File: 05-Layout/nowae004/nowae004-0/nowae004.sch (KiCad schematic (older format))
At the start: 30 parts

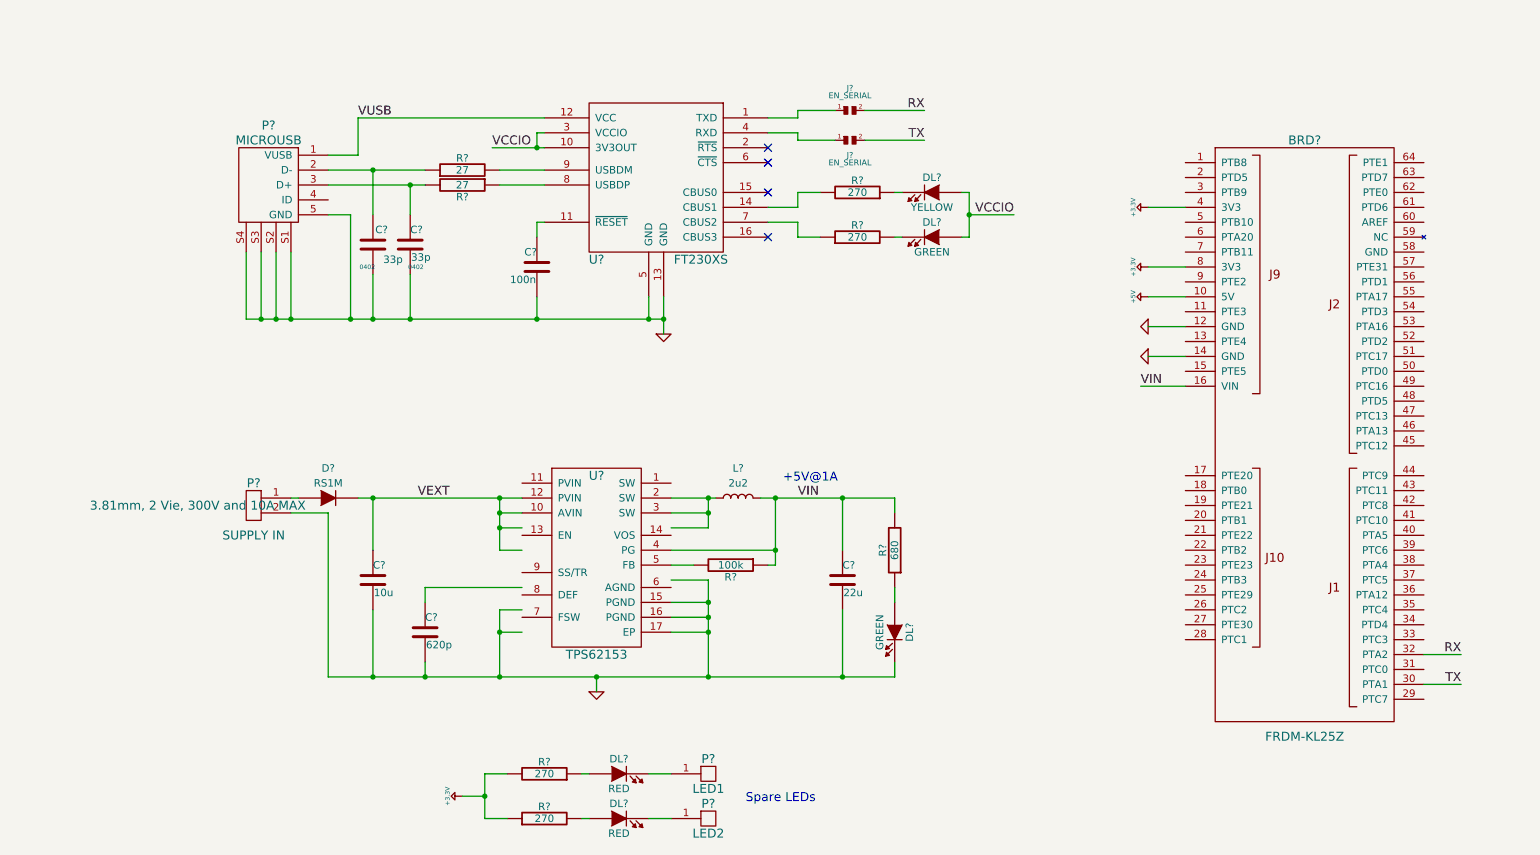
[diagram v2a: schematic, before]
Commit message: Added enumeration into schematich
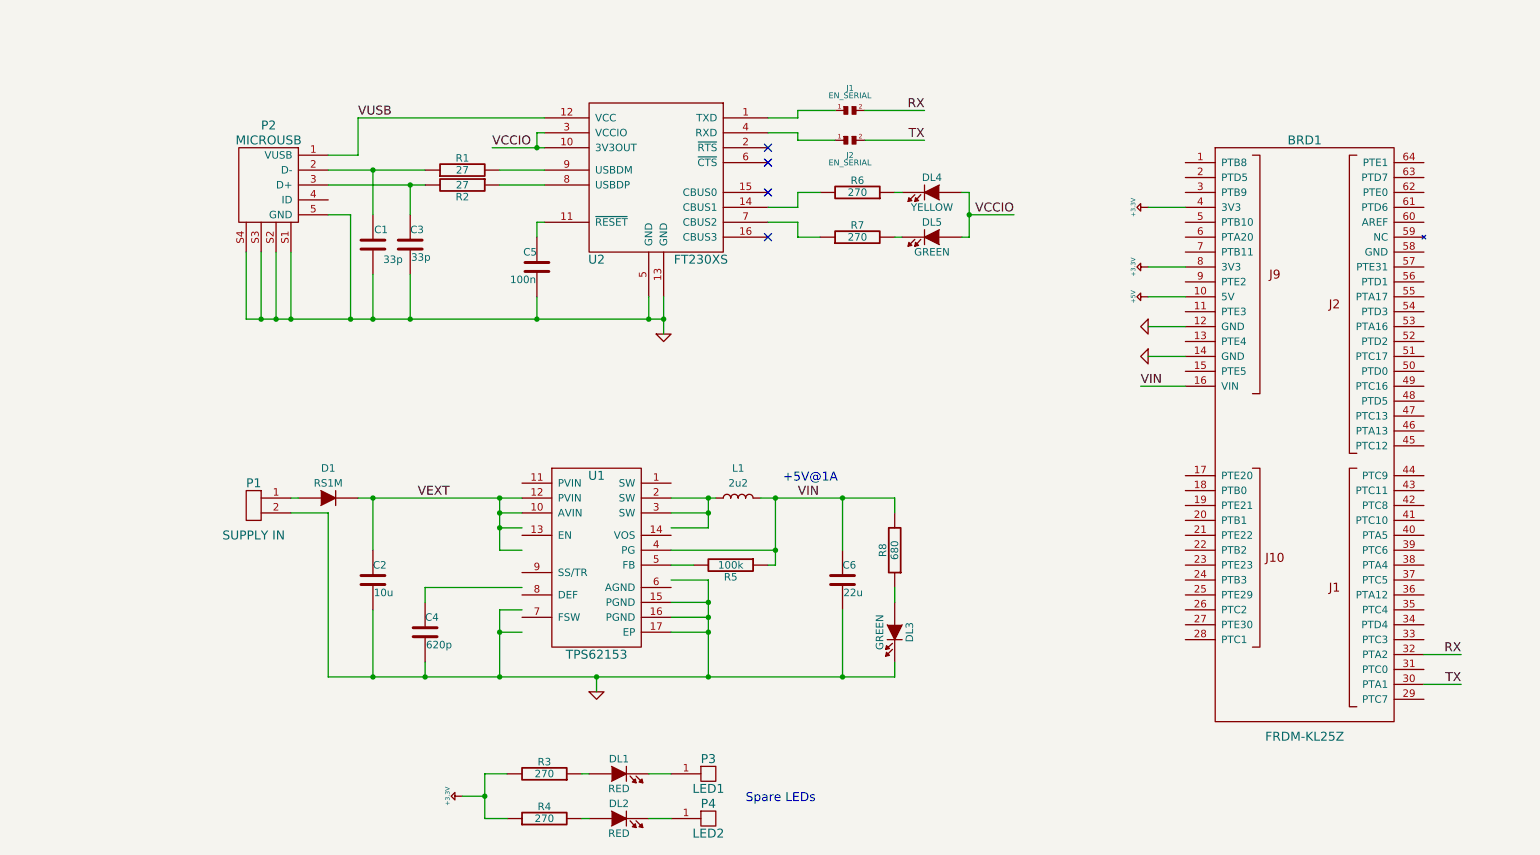
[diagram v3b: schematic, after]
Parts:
- gave numbers to parts that had none: 30
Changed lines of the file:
@@
 Comment2 "Nicola Orlandini"
 Comment3 "Nicola Orlandini"
-Comment4 "2017-02-24"
+Comment4 "2017-02-28"
 $EndDescr
 $Comp
-L GREEN DL?
+L GREEN DL5
 U 1 1 589DB2EE
 P 8500 4000
-F 0 "DL?" H 8500 4100 50  0000 C CNN
+F 0 "DL5" H 8500 4100 50  0000 C CNN
 F 1 "GREEN" H 8500 3900 50  0000 C CNN
 F 2 "0603" H 8500 4000 60  0001 C CNN
@@
 $EndComp
 $Comp
-L YELLOW DL?
+L YELLOW DL4
 U 1 1 589DB33F
 P 8500 3700
-F 0 "DL?" H 8500 3800 50  0000 C CNN
+F 0 "DL4" H 8500 3800 50  0000 C CNN
 F 1 "YELLOW" H 8500 3600 50  0000 C CNN
 F 2 "" H 8500 3700 60  0001 C CNN
@@
 $EndComp
 $Comp
-L RESISTOR R?
+L RESISTOR R7
 U 1 1 589DBA27
 P 8000 4000
-F 0 "R?" V 8080 4000 50  0000 C CNN
+F 0 "R7" V 8080 4000 50  0000 C CNN
 F 1 "270" V 8000 4000 50  0000 C CNN
 F 2 "0402" V 7930 4000 30  0001 C CNN
@@
 VCCIO
 $Comp
-L CAPACITOR C?
+L CAPACITOR C5
 U 1 1 589DBD48
 P 5850 4200
-F 0 "C?" H 5850 4300 50  0000 L CNN
+F 0 "C5" H 5850 4300 50  0000 L CNN
 F 1 "100n" H 5856 4115 50  0000 L CNN
 F 2 "0402" H 5888 4050 30  0001 C CNN
@@
 	6600 4550 6700 4550
 $Comp
-L RESISTOR R?
+L RESISTOR R2
 U 1 1 589DC009
 P 5350 3650
-F 0 "R?" V 5430 3650 50  0000 C CNN
+F 0 "R2" V 5430 3650 50  0000 C CNN
 F 1 "27" V 5350 3650 50  0000 C CNN
 F 2 "0402" V 5280 3650 30  0001 C CNN
@@
 $EndComp
 $Comp
-L RESISTOR R?
+L RESISTOR R1
 U 1 1 589DC06A
 P 5350 3550
-F 0 "R?" V 5430 3550 50  0000 C CNN
+F 0 "R1" V 5430 3550 50  0000 C CNN
 F 1 "27" V 5350 3550 50  0000 C CNN
 F 2 "0402" V 5280 3550 30  0001 C CNN
@@
 $EndComp
 $Comp
-L CAPACITOR C?
+L CAPACITOR C3
 U 1 1 589DC137
 P 5000 4050
-F 0 "C?" H 5000 4150 50  0000 L CNN
+F 0 "C3" H 5000 4150 50  0000 L CNN
 F 1 "33p" H 5006 3965 50  0000 L CNN
-F 2 "0402" H 5038 3900 30  0000 C CNN
+F 2 "0402" H 5038 3900 30  0001 C CNN
 F 3 "" H 5000 4050 60  0000 C CNN
 F 4 "Multicomp" H 4550 5950 60  0001 C CNN "Manufacturer"
@@
 $EndComp
 $Comp
-L CAPACITOR C?
+L CAPACITOR C1
 U 1 1 589DC176
 P 4750 4050
-F 0 "C?" H 4650 4150 50  0000 L CNN
+F 0 "C1" H 4650 4150 50  0000 L CNN
 F 1 "33p" H 4550 3950 50  0000 L CNN
-F 2 "0402" H 4788 3900 30  0000 C CNN
+F 2 "0402" H 4788 3900 30  0001 C CNN
 F 3 "" H 4750 4050 60  0000 C CNN
 F 4 "Multicomp" H 4550 5950 60  0001 C CNN "Manufacturer"
@@
 Connection ~ 5000 4550
 $Comp
-L RESISTOR R?
+L RESISTOR R6
 U 1 1 589DB816
 P 8000 3700
-F 0 "R?" V 8080 3700 50  0000 C CNN
+F 0 "R6" V 8080 3700 50  0000 C CNN
 F 1 "270" V 8000 3700 50  0000 C CNN
 F 2 "0402" V 7930 3700 30  0001 C CNN
@@
 	7600 3350 7850 3350
 $Comp
-L SMALL_JUMPER J?
+L SMALL_JUMPER J2
 U 1 1 58ACFDE1
 P 7950 3350
-F 0 "J?" H 7950 3250 39  0000 C CNN
+F 0 "J2" H 7950 3250 39  0000 C CNN
 F 1 "EN_SERIAL" H 7950 3200 39  0000 C CNN
 F 2 "" H 7950 3350 60  0000 C CNN
@@
 $EndComp
 $Comp
-L SMALL_JUMPER J?
+L SMALL_JUMPER J1
 U 1 1 58AD00EA
 P 7950 3150
-F 0 "J?" H 7950 3300 39  0000 C CNN
+F 0 "J1" H 7950 3300 39  0000 C CNN
 F 1 "EN_SERIAL" H 7950 3250 39  0000 C CNN
 F 2 "" H 7950 3150 60  0000 C CNN
@@
 Connection ~ 6700 4550
 $Comp
-L GND #PWR?
+L GND #PWR3
 U 1 1 58AD26EE
 P 6700 4650
-F 0 "#PWR?" H 6700 4650 30  0001 C CNN
+F 0 "#PWR3" H 6700 4650 30  0001 C CNN
 F 1 "GND" H 6700 4650 30  0001 C CNN
 F 2 "" H 6700 4650 60  0000 C CNN
@@
 	4600 3850 4600 4550
 $Comp
-L FRDM-KL25Z BRD?
+L FRDM-KL25Z BRD1
 U 1 1 58AD8FDC
 P 11000 5500
-F 0 "BRD?" H 11000 7650 60  0000 C CNN
+F 0 "BRD1" H 11000 7650 60  0000 C CNN
 F 1 "FRDM-KL25Z" H 11000 3650 60  0000 C CNN
 F 2 "" H 10700 5900 60  0000 C CNN
@@
 	10200 4800 9950 4800
 $Comp
-L GND #PWR?
+L GND #PWR7
 U 1 1 58AD94F9
 P 9950 4600
-F 0 "#PWR?" H 9950 4600 30  0001 C CNN
+F 0 "#PWR7" H 9950 4600 30  0001 C CNN
 F 1 "GND" H 9950 4600 30  0001 C CNN
 F 2 "" H 9950 4600 60  0000 C CNN
@@
 $EndComp
 $Comp
-L GND #PWR?
+L GND #PWR8
 U 1 1 58AD9532
 P 9950 4800
-F 0 "#PWR?" H 9950 4800 30  0001 C CNN
+F 0 "#PWR8" H 9950 4800 30  0001 C CNN
 F 1 "GND" H 9950 4800 30  0001 C CNN
 F 2 "" H 9950 4800 60  0000 C CNN
@@
 	10200 3800 9950 3800
 $Comp
-L +3.3V #PWR?
+L +3.3V #PWR4
 U 1 1 58AD96A9
 P 9950 3800
-F 0 "#PWR?" H 9950 3725 30  0001 C CNN
+F 0 "#PWR4" H 9950 3725 30  0001 C CNN
 F 1 "+3.3V" H 9950 3900 30  0000 C CNN
 F 2 "" H 9950 3800 60  0000 C CNN
@@
 $EndComp
 $Comp
-L +3.3V #PWR?
+L +3.3V #PWR5
 U 1 1 58AD96E2
 P 9950 4200
-F 0 "#PWR?" H 9950 4125 30  0001 C CNN
+F 0 "#PWR5" H 9950 4125 30  0001 C CNN
 F 1 "+3.3V" H 9950 4300 30  0000 C CNN
 F 2 "" H 9950 4200 60  0000 C CNN
@@
 $EndComp
 $Comp
-L +5V #PWR?
+L +5V #PWR6
 U 1 1 58AD9709
 P 9950 4400
-F 0 "#PWR?" H 9950 4325 30  0001 C CNN
+F 0 "#PWR6" H 9950 4325 30  0001 C CNN
 F 1 "+5V" H 9950 4500 30  0000 C CNN
 F 2 "" H 9950 4400 60  0000 C CNN
@@
 $EndComp
 $Comp
-L MICROUSB-629105150521 P?
+L MICROUSB-629105150521 P2
 U 1 1 58AD9919
 P 4050 3650
-F 0 "P?" H 4050 4050 60  0000 C CNN
+F 0 "P2" H 4050 4050 60  0000 C CNN
 F 1 "MICROUSB" H 4050 3950 60  0000 C CNN
 F 2 "" H 4425 3650 60  0000 C CNN
@@
 Connection ~ 4200 4550
 $Comp
-L TPS62153 U?
+L TPS62153 U1
 U 1 1 58AED925
 P 6250 6200
-F 0 "U?" H 6250 6800 60  0000 C CNN
+F 0 "U1" H 6250 6800 60  0000 C CNN
 F 1 "TPS62153" H 6250 5600 60  0000 C CNN
 F 2 "VQFN16" H 6250 5100 60  0001 C CNN
@@
 $EndComp
 $Comp
-L CONN_2X1 P?
+L CONN_2X1 P1
 U 1 1 58AEDA14
 P 3950 5800
-F 0 "P?" H 3950 5950 60  0000 C CNN
+F 0 "P1" H 3950 5950 60  0000 C CNN
 F 1 "SUPPLY IN" H 3950 5600 60  0000 C CNN
 F 2 "" H 4325 5800 60  0000 C CNN
-F 3 "3.81mm, 2 Vie, 300V and 10A MAX " H 4325 5800 60  0000 C CNN
+F 3 "3.81mm, 2 Vie, 300V and 10A MAX " H 4325 5800 60  0001 C CNN
 F 4 "Multicomp" H 4550 5950 60  0001 C CNN "Manufacturer"
 F 5 "MC000018" H 4650 6050 60  0001 C CNN "Part Number"
@@
 Connection ~ 5600 6950
 $Comp
-L CAPACITOR C?
+L CAPACITOR C2
 U 1 1 58AEDD67
 P 4750 6300
-F 0 "C?" H 4750 6400 50  0000 L CNN
+F 0 "C2" H 4750 6400 50  0000 L CNN
 F 1 "10u" H 4756 6215 50  0000 L CNN
 F 2 "1206" H 4788 6150 30  0001 C CNN
@@
 Connection ~ 4750 6950
 $Comp
-L CAPACITOR C?
+L CAPACITOR C4
 U 1 1 58AEDFEA
 P 5100 6650
-F 0 "C?" H 5100 6750 50  0000 L CNN
+F 0 "C4" H 5100 6750 50  0000 L CNN
 F 1 "620p" H 5106 6565 50  0000 L CNN
 F 2 "0805" H 5138 6500 30  0001 C CNN
@@
 Connection ~ 7000 6450
 $Comp
-L CAPACITOR C?
+L CAPACITOR C6
 U 1 1 58AEE473
 P 7900 6300
-F 0 "C?" H 7900 6400 50  0000 L CNN
+F 0 "C6" H 7900 6400 50  0000 L CNN
 F 1 "22u" H 7906 6215 50  0000 L CNN
 F 2 "1206" H 7938 6150 30  0001 C CNN
@@
 Connection ~ 7000 6950
 $Comp
-L INDUCTOR L?
+L INDUCTOR L1
 U 1 1 58AEE57C
 P 7200 5750
-F 0 "L?" V 7400 5750 50  0000 C CNN
+F 0 "L1" V 7400 5750 50  0000 C CNN
 F 1 "2u2" V 7300 5750 50  0000 C CNN
 F 2 "" H 7200 5750 60  0000 C CNN
@@
 Connection ~ 7450 5750
 $Comp
-L RESISTOR R?
+L RESISTOR R5
 U 1 1 58AEE920
 P 7150 6200
-F 0 "R?" V 7230 6200 50  0000 C CNN
+F 0 "R5" V 7230 6200 50  0000 C CNN
 F 1 "100k" V 7150 6200 50  0000 C CNN
 F 2 "0402" V 7080 6200 30  0001 C CNN
@@
 Connection ~ 6250 6950
 $Comp
-L GND #PWR?
+L GND #PWR2
 U 1 1 58AEEF34
 P 6250 7050
-F 0 "#PWR?" H 6250 7050 30  0001 C CNN
+F 0 "#PWR2" H 6250 7050 30  0001 C CNN
 F 1 "GND" H 6250 7050 30  0001 C CNN
 F 2 "" H 6250 7050 60  0000 C CNN
@@
 Connection ~ 7900 5750
 $Comp
-L RESISTOR R?
+L RESISTOR R8
 U 1 1 58AEFD7A
 P 8250 6100
-F 0 "R?" V 8330 6100 50  0000 C CNN
+F 0 "R8" V 8330 6100 50  0000 C CNN
 F 1 "680" V 8250 6100 50  0000 C CNN
 F 2 "0402" V 8180 6100 30  0001 C CNN
@@
 	8250 5750 8250 5850
 $Comp
-L GREEN DL?
+L GREEN DL3
 U 1 1 58AEFE67
 P 8250 6650
-F 0 "DL?" H 8250 6750 50  0000 C CNN
+F 0 "DL3" H 8250 6750 50  0000 C CNN
 F 1 "GREEN" H 8250 6550 50  0000 C CNN
 F 2 "" H 8250 6650 60  0001 C CNN
@@
 	8250 6450 8250 6350
 $Comp
-L FT230XS U?
+L FT230XS U2
 U 1 1 58AF0874
 P 6650 3600
-F 0 "U?" H 6250 3050 60  0000 C CNN
+F 0 "U2" H 6250 3050 60  0000 C CNN
 F 1 "FT230XS" H 6950 3050 60  0000 C CNN
 F 2 "SSOP16" H 7000 4750 60  0001 C CNN
@@
 	4650 3200 5900 3200
 $Comp
-L RESISTOR R?
+L RESISTOR R4
 U 1 1 58B03137
 P 5900 7900
-F 0 "R?" V 5980 7900 50  0000 C CNN
+F 0 "R4" V 5980 7900 50  0000 C CNN
 F 1 "270" V 5900 7900 50  0000 C CNN
 F 2 "0402" V 5830 7900 30  0001 C CNN
@@
 	6150 7900 6200 7900
 $Comp
-L RESISTOR R?
+L RESISTOR R3
 U 1 1 58B03144
 P 5900 7600
-F 0 "R?" V 5980 7600 50  0000 C CNN
+F 0 "R3" V 5980 7600 50  0000 C CNN
 F 1 "270" V 5900 7600 50  0000 C CNN
 F 2 "0402" V 5830 7600 30  0001 C CNN
@@
 	5500 7900 5650 7900
 $Comp
-L RED DL?
+L RED DL1
 U 1 1 58B03399
 P 6400 7600
-F 0 "DL?" H 6400 7700 50  0000 C CNN
+F 0 "DL1" H 6400 7700 50  0000 C CNN
 F 1 "RED" H 6400 7500 50  0000 C CNN
 F 2 "0603" H 6400 7600 60  0001 C CNN
@@
 $EndComp
 $Comp
-L RED DL?
+L RED DL2
 U 1 1 58B03403
 P 6400 7900
-F 0 "DL?" H 6400 8000 50  0000 C CNN
+F 0 "DL2" H 6400 8000 50  0000 C CNN
 F 1 "RED" H 6400 7800 50  0000 C CNN
 F 2 "0603" H 6400 7900 60  0001 C CNN
@@
 Connection ~ 5500 7750
 $Comp
-L +3.3V #PWR?
+L +3.3V #PWR1
 U 1 1 58B03696
 P 5350 7750
-F 0 "#PWR?" H 5350 7675 30  0001 C CNN
+F 0 "#PWR1" H 5350 7675 30  0001 C CNN
 F 1 "+3.3V" H 5350 7850 30  0000 C CNN
 F 2 "" H 5350 7750 60  0000 C CNN
@@
 Spare LEDs
 $Comp
-L CONN_1X1 P?
+L CONN_1X1 P3
 U 1 1 58B04044
 P 7000 7600
-F 0 "P?" H 7000 7700 60  0000 C CNN
+F 0 "P3" H 7000 7700 60  0000 C CNN
 F 1 "LED1" H 7000 7500 60  0000 C CNN
 F 2 "" H 7375 7600 60  0000 C CNN
@@
 $EndComp
 $Comp
-L CONN_1X1 P?
+L CONN_1X1 P4
 U 1 1 58B041D9
 P 7000 7900
-F 0 "P?" H 7000 8000 60  0000 C CNN
+F 0 "P4" H 7000 8000 60  0000 C CNN
 F 1 "LED2" H 7000 7800 60  0000 C CNN
 F 2 "" H 7000 7700 60  0001 C CNN
@@
 $EndComp
 $Comp
-L RS1M D?
+L RS1M D1
 U 1 1 58B0468B
 P 4450 5750
-F 0 "D?" H 4450 5950 50  0000 C CNN
+F 0 "D1" H 4450 5950 50  0000 C CNN
 F 1 "RS1M" H 4450 5850 50  0000 C CNN
 F 2 "" H 4450 5750 60  0001 C CNN

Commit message: NOWAE004: Changed symbol of switching component
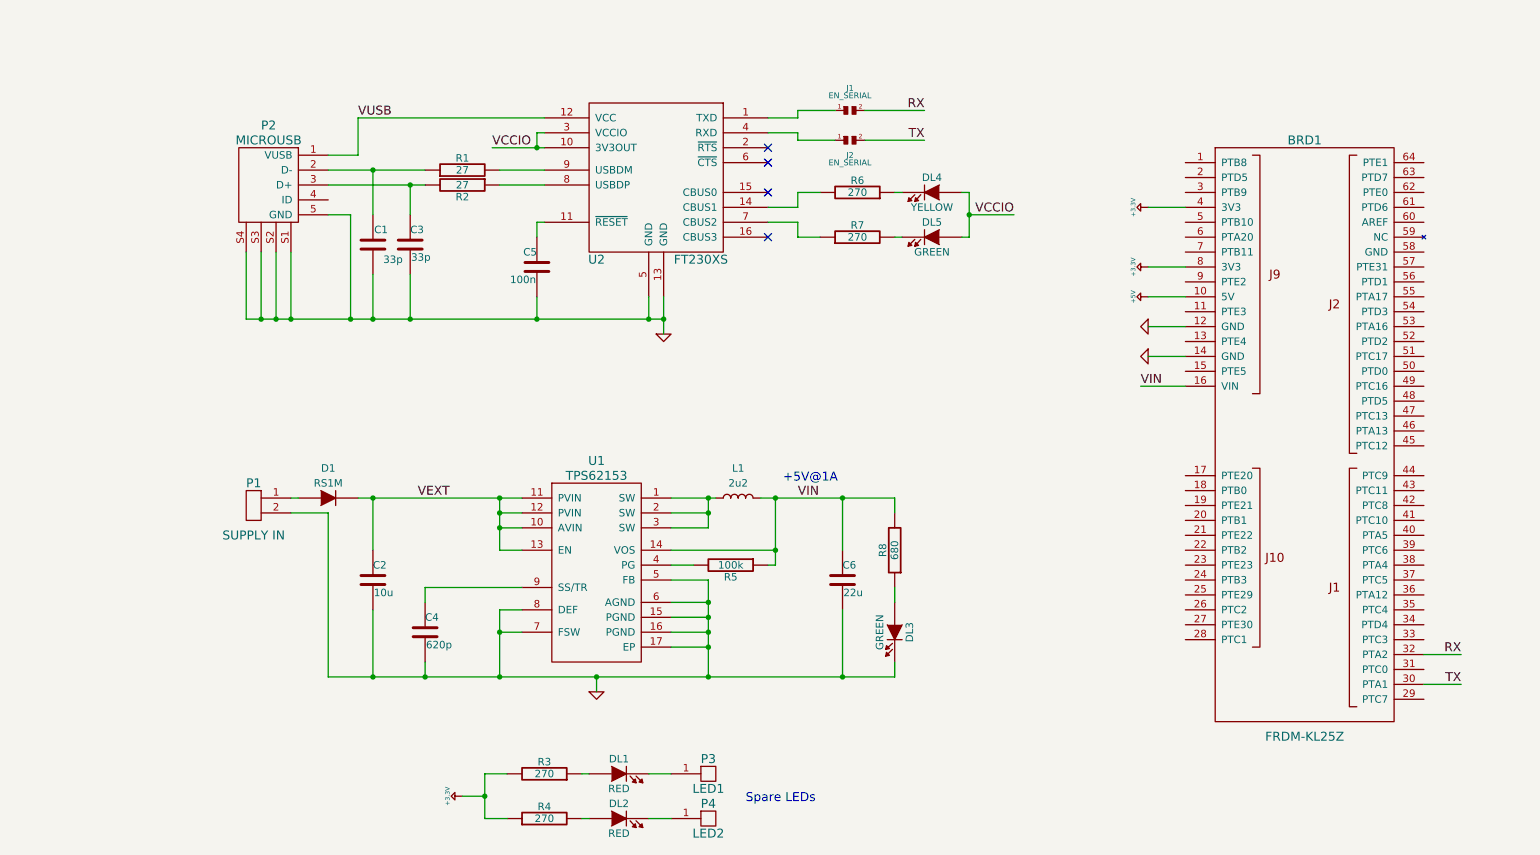
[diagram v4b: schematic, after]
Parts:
- BRD1: footprint (none) -> CONNECTOR:CONN-FRDM
- C1, C3, C5: footprint 0402 -> CAPACITOR:CAPACITOR-0402
- C2, C6: footprint 1206 -> CAPACITOR:CAPACITOR-1206
- C4: footprint 0805 -> CAPACITOR:CAPACITOR-0402
- D1: footprint (none) -> DIODE:DIODE-DO214AC-UNI
- DL1, DL2, DL5: footprint 0603 -> LEDs:LED-0603
- DL3, DL4: footprint (none) -> LEDs:LED-0603
- L1: footprint (none) -> INDUCTOR:INDUCTOR-TDK-SPM3012
- P1: footprint (none) -> CONNECTOR_MKDS:CONN-MKDS1_2-3.81
- P2: footprint (none) -> CONNECTOR:MICROUSB-WURTH-WRCOM
- R1, R2, R3, R4, R5, R6, R7, R8: footprint 0402 -> RESISTOR:RESISTOR-0402
- U1: footprint VQFN16 -> QFN:QFN16_3x3_0.5_16+1
- U2: footprint SSOP16 -> SSOP:SSOP16_3.9x4.9_0.635
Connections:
- wire segments 132 -> 100

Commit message: NOWAE004: Added last footprint and updated netlist
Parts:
- J1, J2: footprint (none) -> MISC:JUMPERSMD-2
- P3, P4: footprint (none) -> CONNECTOR:CONN-HOLE-1.2
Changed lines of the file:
@@
 F 0 "J2" H 7950 3250 39  0000 C CNN
 F 1 "EN_SERIAL" H 7950 3200 39  0000 C CNN
-F 2 "" H 7950 3350 60  0001 C CNN
+F 2 "MISC:JUMPERSMD-2" H 7950 3350 60  0001 C CNN
 F 3 "" H 7950 3350 60  0000 C CNN
 	1    7950 3350
@@
 F 0 "J1" H 7950 3300 39  0000 C CNN
 F 1 "EN_SERIAL" H 7950 3250 39  0000 C CNN
-F 2 "" H 7950 3150 60  0001 C CNN
+F 2 "MISC:JUMPERSMD-2" H 7950 3150 60  0001 C CNN
 F 3 "" H 7950 3150 60  0000 C CNN
 	1    7950 3150
@@
 F 0 "P3" H 7000 7700 60  0000 C CNN
 F 1 "LED1" H 7000 7500 60  0000 C CNN
-F 2 "" H 7375 7600 60  0001 C CNN
+F 2 "CONNECTOR:CONN-HOLE-1.2" H 7375 7600 60  0001 C CNN
 F 3 "" H 7375 7600 60  0000 C CNN
 	1    7000 7600
@@
 F 0 "P4" H 7000 8000 60  0000 C CNN
 F 1 "LED2" H 7000 7800 60  0000 C CNN
-F 2 "" H 7000 7700 60  0001 C CNN
+F 2 "CONNECTOR:CONN-HOLE-1.2" H 7000 7700 60  0001 C CNN
 F 3 "" H 7375 7900 60  0000 C CNN
 	1    7000 7900
